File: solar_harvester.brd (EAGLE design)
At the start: 46 x 25.4 mm, 45 parts, among them U1 BQ25505, U2 TPS61322XA, U3 TPS61322XA, U4 MAX17040, U5 INA226, U6 DMP3085LSD

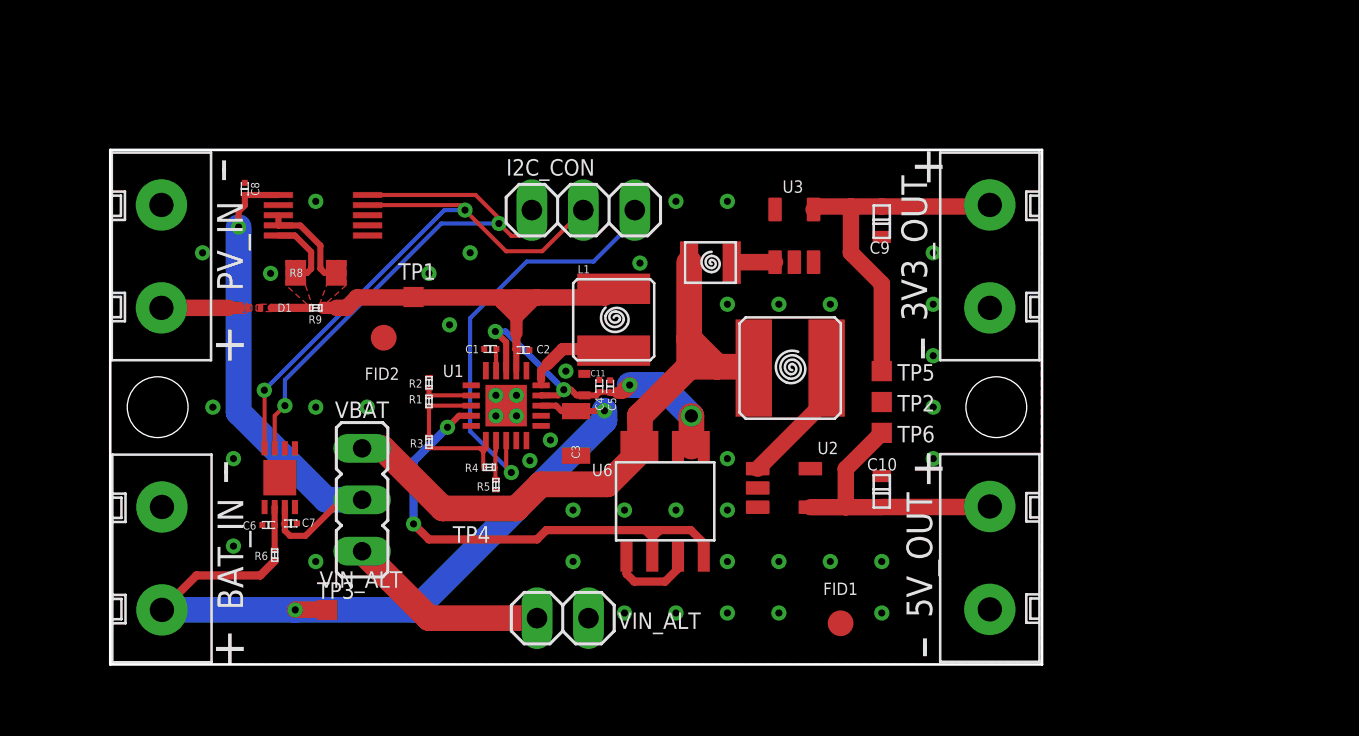
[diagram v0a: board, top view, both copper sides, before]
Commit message: increase comps sizes -> pcb reruting (in progress)
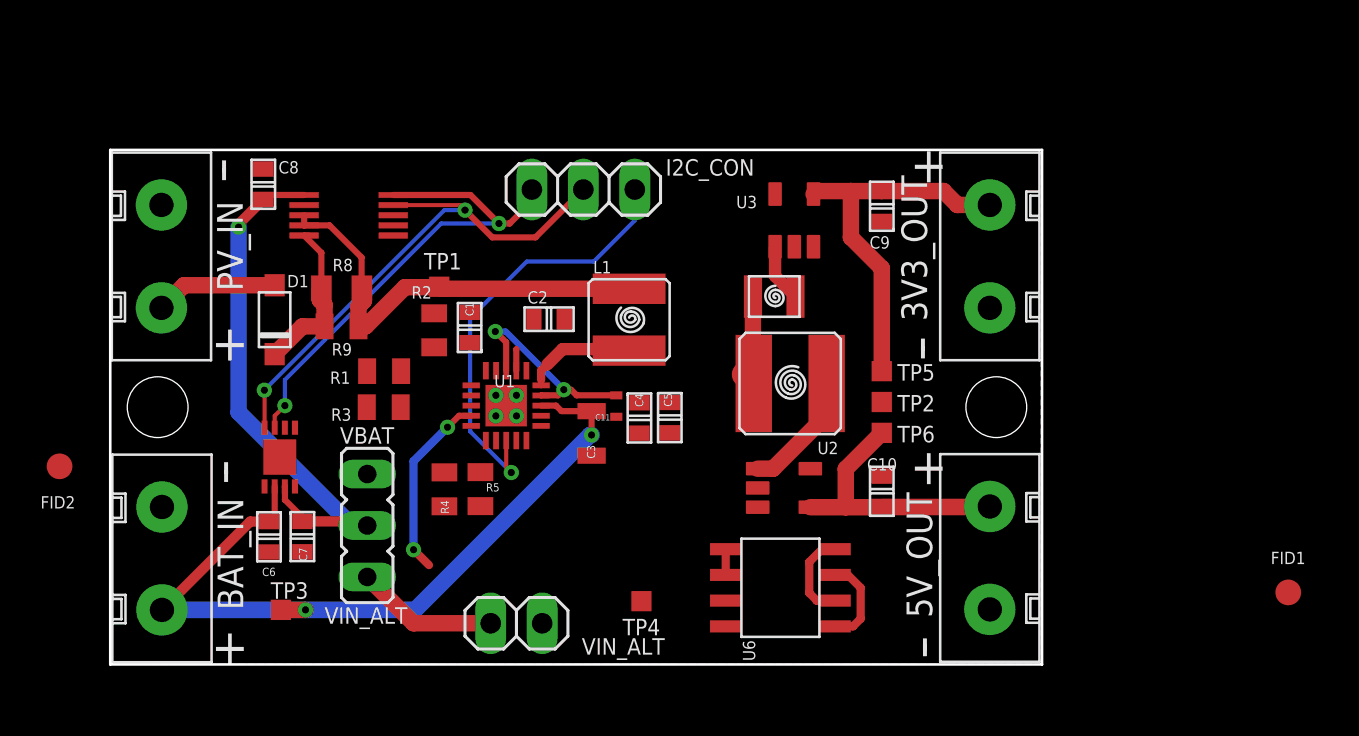
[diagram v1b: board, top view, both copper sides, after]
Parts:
- removed R6: 1K, vrlib_res:RESISTOR_0603_FOOTPRINT
- C1, C2, C4, C5, C6, C7, C8: device vrlib_caps:0603_FOOTPRINT -> vrlib_caps:1608_FOOTPRINT
- D1: value JDH2S02SL -> SD101BW; device vrlib_diode:SOD-962___(SL2) -> vrlib_diode:SOD-123
- R1, R2, R3, R4, R5, R9: device vrlib_res:RESISTOR_0603_FOOTPRINT -> vrlib_res:RESISTOR_1608_FOOTPRINT
- moved FID1 22.2 mm to (58.2, 3.56)
- moved FID2 17.2 mm to (-2.49, 9.78)
- moved TP4 9.55 mm to (26.2, 3.12)
- moved U6 7.11 mm to (33.1, 3.78), turned to 90 degrees
- moved L3 3.57 mm to (32.8, 18.2)
- moved C5 3.32 mm to (27.6, 12.2), turned to 0 degrees
- moved R3 2.82 mm to (13.5, 12.7), turned to 90 degrees
- moved R1 2.67 mm to (13.5, 14.5), turned to 90 degrees
- moved R2 2.60 mm to (16.0, 16.5), turned to 180 degrees
- moved C4 2.53 mm to (26.1, 12.2), turned to 0 degrees
- moved R4 2.47 mm to (16.5, 8.64), turned to 0 degrees
- moved JP3 2.30 mm to (20.1, 2.03)
- moved TP3 2.29 mm to (8.44, 2.69)
- moved C2 1.98 mm to (21.7, 17.0)
- moved C11 1.90 mm to (25.0, 12.8), turned to 0 degrees
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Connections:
- removed net N$8: C6.1, R6.2, U4.2
- net VIN_BAT: now also C6.1, U4.2; no longer R6.1
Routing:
- net VCC: track 34.4 -> 4.65 mm
- net !VB_SEC_ON!: track 25.5 -> 14.6 mm
- net VCC_P: track 18.0 -> 11.9 mm, vias 4 -> 2
- net N$5: track 4.46 -> 0.00 mm
- net N$3: track 3.53 -> 0.00 mm
- net PVIN_AN: track 26.2 -> 22.8 mm
- net VIN_ALT: track 10.0 -> 7.04 mm
- net PVIN: track 5.52 -> 8.22 mm
- net I2C_SCL: track 27.4 -> 24.8 mm
- net I2C_SDA: track 28.9 -> 26.5 mm
- net N$4: track 2.41 -> 0.00 mm
- net N$7: track 3.81 -> 6.05 mm
- net N$8: track 2.08 -> 0.00 mm
- net N$6: track 1.90 -> 0.00 mm
- net VIN_BAT: track 37.6 -> 38.7 mm
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- removed copper zone on layer 1, net N$7
- removed copper zone on layer 1, net PVIN
- removed copper zone on layer 1, net PVIN_AN

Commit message: rerouting finished
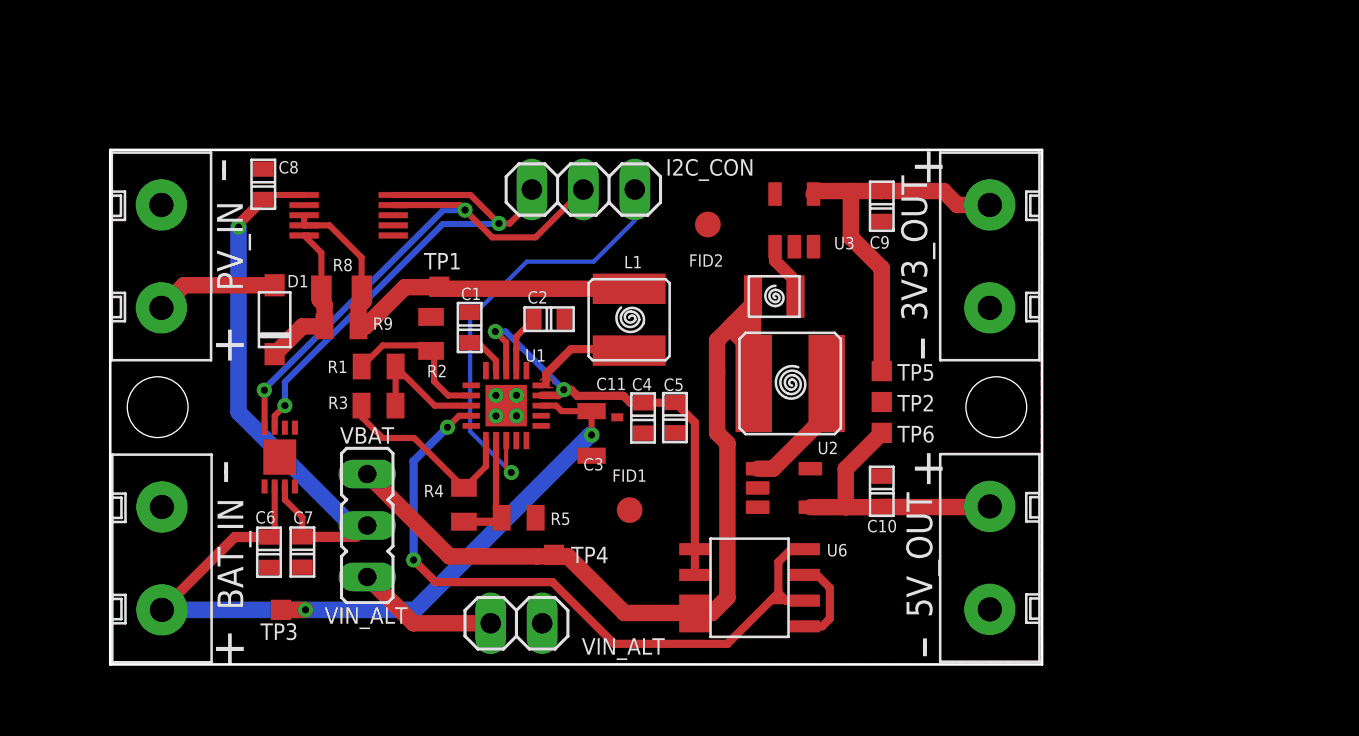
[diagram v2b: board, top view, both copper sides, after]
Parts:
- moved FID2 34.2 mm to (29.5, 21.7)
- moved FID1 32.8 mm to (25.7, 7.62)
- moved TP4 4.89 mm to (21.9, 5.41)
- moved R5 2.36 mm to (20.2, 7.24), turned to 90 degrees
- moved U6 1.52 mm to (31.6, 3.78)
- moved R4 1.23 mm to (17.5, 7.88)
- moved C6 0.76 mm to (7.85, 5.54)
- moved C7 0.76 mm to (9.50, 5.55)
- moved R1 0.35 mm to (13.3, 14.7), turned to 270 degrees
- moved R3 0.27 mm to (13.3, 12.8), turned to 270 degrees
- moved C5 0.25 mm to (27.9, 12.2)
- moved R2 0.23 mm to (15.8, 16.3)
- moved C4 0.18 mm to (26.3, 12.2)
- moved C11 0.06 mm to (25.0, 12.7)
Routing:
- net VCC: track 4.65 -> 44.6 mm
- net !VB_SEC_ON!: track 14.6 -> 35.1 mm
- net VCC_P: track 11.9 -> 22.6 mm
- net N$5: track 0.00 -> 9.86 mm
- net N$4: track 0.00 -> 7.68 mm
- net N$3: track 0.00 -> 6.46 mm
- net N$6: track 0.00 -> 5.84 mm
- net N$2: track 0.00 -> 2.17 mm
- net PVIN_AN: track 22.8 -> 24.7 mm
- net VCC_MIX: track 27.2 -> 28.1 mm
- added copper zone on layer 1, net N$1

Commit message: Rev 1 done. todo: bom update
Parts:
- moved C2 0.85 mm to (21.7, 17.9), turned to 0 degrees
- moved FID1 0.51 mm to (25.7, 7.11)
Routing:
- net PVIN_AN: track 24.7 -> 27.8 mm
- net VCC: track 44.6 -> 45.5 mm
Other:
- board text added: "L2"
- board text added: "Rev 1"
- board text removed: "Rev 0"

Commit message: BOM updated
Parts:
- R3: value 7.32M -> 1.2M
- R4: value 7.32M -> 7.5M
- R5: value 7.32M -> 4.3M
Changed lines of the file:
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@@
 <attribute name="NAME" x="15.6436" y="14.1744" size="0.6096" layer="25"/>
 </element>
-<element name="R3" library="vrlib_res" package="RESISTOR_1608_FOOTPRINT" value="7.32M" x="13.2574" y="12.7762" smashed="yes" rot="R270">
+<element name="R3" library="vrlib_res" package="RESISTOR_1608_FOOTPRINT" value="1.2M" x="13.2574" y="12.7762" smashed="yes" rot="R270">
 <attribute name="NAME" x="11.763" y="13.2226" size="0.6096" layer="25" rot="R180"/>
 </element>
-<element name="R4" library="vrlib_res" package="RESISTOR_1608_FOOTPRINT" value="7.32M" x="17.4752" y="7.8822" smashed="yes">
+<element name="R4" library="vrlib_res" package="RESISTOR_1608_FOOTPRINT" value="7.5M" x="17.4752" y="7.8822" smashed="yes">
 <attribute name="NAME" x="16.4874" y="8.8696" size="0.6096" layer="25" rot="R180"/>
 </element>
-<element name="R5" library="vrlib_res" package="RESISTOR_1608_FOOTPRINT" value="7.32M" x="20.1752" y="7.239" smashed="yes" rot="R90">
+<element name="R5" library="vrlib_res" package="RESISTOR_1608_FOOTPRINT" value="4.3M" x="20.1752" y="7.239" smashed="yes" rot="R90">
 <attribute name="NAME" x="21.7396" y="6.888" size="0.6096" layer="25"/>
 </element>

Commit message: Rev2
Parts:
- removed 3V3_OUT, 5V_OUT, BAT_IN, PV_IN: CONN_SCEW_TYPE_2P, vrlib_connector:CONN_SCREW_TYPE_2P
- added +BAT_IN--, +PV_IN--, --3V3_OUT+, --5V_OUT+: CONN_SCEW_TYPE_2P, vrlib_connector:CONN_SCREW_TYPE_2P
- added FID3, FID4: FIDUCIAL_25, vrlib_prod:FIDUCIAL_25
- C10, C9: value 22u -> 100u; device vrlib_caps:1608_FOOTPRINT -> vrlib_caps:3528_TAN_FOOTPRINT
- C11: device vrlib_caps:1005_FOOTPRINT -> vrlib_caps:1608_FOOTPRINT
- C3: device vrlib_caps:2012_FOOTPRINT -> vrlib_caps:3528_TAN_FOOTPRINT
- moved FID1 27.2 mm to (52.8, 5.97)
- moved FID2 23.6 mm to (52.8, 25.6)
- moved TP3 23.0 mm to (30.3, 9.78)
- moved JP4 13.8 mm to (25.9, 2.62), turned to 180 degrees
- moved C8 11.5 mm to (17.7, 29.1), turned to 90 degrees
- moved TP5 10.2 mm to (36.0, 24.5)
- moved C10 10.0 mm to (46.6, 13.9), turned to 270 degrees
- moved C9 9.87 mm to (46.6, 17.6), turned to 270 degrees
- moved TP4 8.80 mm to (30.3, 8.03)
- moved TP1 8.46 mm to (23.6, 22.8)
- moved U4 8.15 mm to (16.5, 9.38), turned to 270 degrees
- moved C4 8.08 mm to (33.5, 15.8), turned to 180 degrees
- moved L1 8.07 mm to (31.9, 22.1)
- moved C7 7.97 mm to (10.1, 13.5), turned to 180 degrees
- moved C6 7.94 mm to (7.93, 13.5), turned to 180 degrees
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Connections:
- net GND: now also +BAT_IN--.2, +PV_IN--.2, --3V3_OUT+.2, --5V_OUT+.2; no longer 3V3_OUT.2, 5V_OUT.2, BAT_IN.2, PV_IN.2
- net N$7: now also +PV_IN--.1; no longer PV_IN.1
- net VDD3V3: now also --3V3_OUT+.1; no longer 3V3_OUT.1
- net VDD5: now also --5V_OUT+.1; no longer 5V_OUT.1
- net VIN_BAT: now also +BAT_IN--.1; no longer BAT_IN.1
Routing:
- net VCC: track 45.5 -> 10.2 mm
- net VCC_MIX: track 28.1 -> 59.2 mm, vias 1 -> 2
- net VIN_BAT: track 39.2 -> 54.9 mm, vias 2 -> 1
- net VDD5: track 13.3 -> 2.38 mm
- net VDD3V3: track 18.6 -> 7.73 mm
- net I2C_SCL: track 24.7 -> 32.8 mm
- net !VB_SEC_ON!: track 35.1 -> 27.2 mm
- net I2C_SDA: track 26.5 -> 33.0 mm
- net N$1: track 5.31 -> 9.09 mm
- net VIN_ALT: track 7.04 -> 3.55 mm
- net PVIN_AN: track 27.8 -> 31.2 mm
- net N$5: track 9.86 -> 7.14 mm
- net PVIN: track 8.00 -> 10.3 mm
- net VCC_P: track 22.6 -> 24.6 mm
- net N$2: track 2.17 -> 3.77 mm
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- added copper zone on layer 1, net VCC
- added copper zone on layer 1, net VDD3V3
- added copper zone on layer 1, net VDD5
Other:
- board size 46 x 25.4 mm -> 54 x 30 mm
- board text added: "Rev 2"
- board text removed: "-"
- board text removed: "I2C_CON"
- board text removed: "Rev 1"
